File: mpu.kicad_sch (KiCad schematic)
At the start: 172 parts, among them J1 USB_OTG, J2 DIN41612_02x10_AB, J3 USB_OTG, J4 Conn_02x20_Counter_Clockwise, J5 Conn_01x15_Socket, U3 ECMF02-2AMX6, U4 ECMF02-2AMX6, U5 STM32MP157FADx, X1 ASE-24MHz

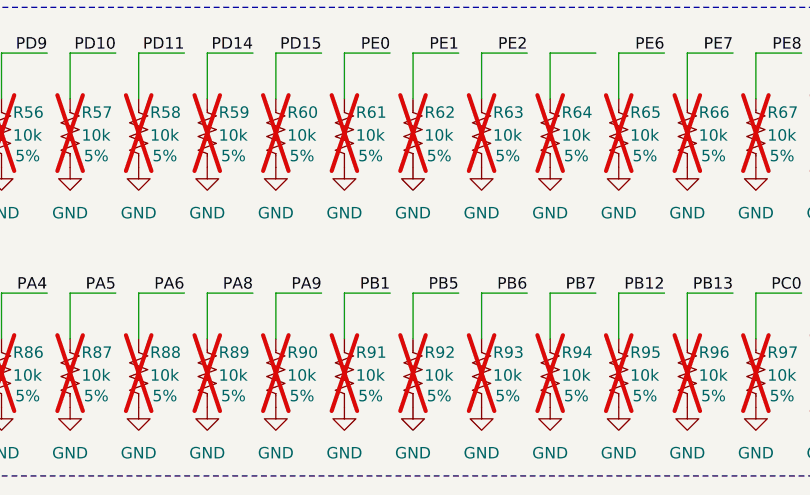
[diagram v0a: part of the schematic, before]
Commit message: Routing GPIOs
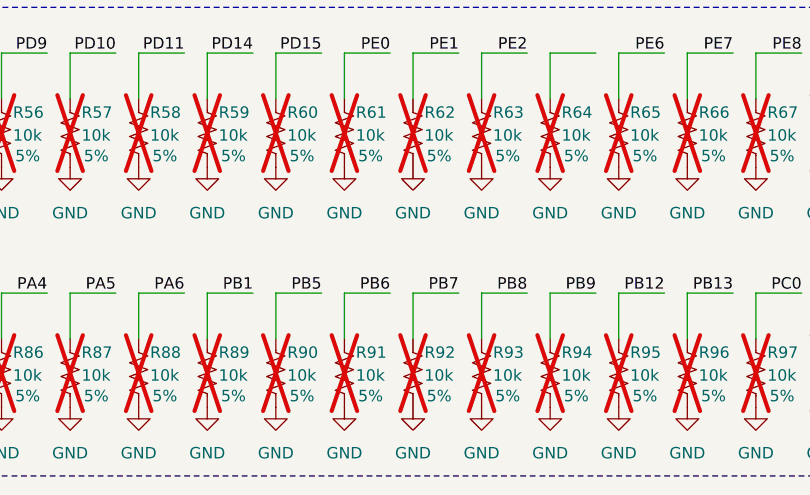
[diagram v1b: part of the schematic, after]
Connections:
- net PA9 is gone; now on net PB5: R90.1
- net PA8: no longer R89.1
- net PB1: now also R89.1; no longer R91.1
- net PB5: no longer R92.1
- net PB6: now also R91.1; no longer R93.1
- net PB7: now also R92.1; no longer R94.1
- net PB8: now also R93.1
- net PB9: now also R94.1
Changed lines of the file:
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@@
 		)
 	)
-	(label "PB7"
-		(at 95.25 397.51 180)
-		(fields_autoplaced yes)
-		(effects
-			(font
-				(size 1.27 1.27)
-			)
-			(justify right bottom)
-		)
-	)
 	(label "UART4_TX"
 		(at 326.39 229.87 0)
@@
 		)
 	)
-	(label "PB6"
-		(at 87.63 397.51 180)
-		(fields_autoplaced yes)
-		(effects
-			(font
-				(size 1.27 1.27)
-			)
-			(justify right bottom)
-		)
-	)
 	(label "PA5"
 		(at 326.39 227.33 0)
@@
 		)
 	)
-	(label "PB1"
-		(at 72.39 397.51 180)
-		(fields_autoplaced yes)
-		(effects
-			(font
-				(size 1.27 1.27)
-			)
-			(justify right bottom)
-		)
-	)
 	(label "PF10"
 		(at 209.55 370.84 180)
@@
 		)
 	)
+	(label "PB1"
+		(at 57.15 397.51 180)
+		(fields_autoplaced yes)
+		(effects
+			(font
+				(size 1.27 1.27)
+			)
+			(justify right bottom)
+		)
+	)
 	(label "nRST"
 		(at 496.57 105.41 0)
@@
 		)
 	)
+	(label "PB8"
+		(at 87.63 397.51 180)
+		(fields_autoplaced yes)
+		(effects
+			(font
+				(size 1.27 1.27)
+			)
+			(justify right bottom)
+		)
+	)
 	(label "A14"
 		(at 196.85 232.41 0)
@@
 		)
 	)
+	(label "PB5"
+		(at 64.77 397.51 180)
+		(fields_autoplaced yes)
+		(effects
+			(font
+				(size 1.27 1.27)
+			)
+			(justify right bottom)
+		)
+	)
 	(label "PC10"
 		(at 171.45 397.51 180)
@@
 		)
 	)
+	(label "PB9"
+		(at 95.25 397.51 180)
+		(fields_autoplaced yes)
+		(effects
+			(font
+				(size 1.27 1.27)
+			)
+			(justify right bottom)
+		)
+	)
 	(label "VDD_DDR"
 		(at 105.41 325.12 90)
@@
 		)
 	)
-	(label "PA8"
-		(at 57.15 397.51 180)
-		(fields_autoplaced yes)
-		(effects
-			(font
-				(size 1.27 1.27)
-			)
-			(justify right bottom)
-		)
-	)
 	(label "VDD_CORE"
 		(at 115.57 325.12 90)
@@
 		)
 	)
-	(label "PA9"
-		(at 64.77 397.51 180)
+	(label "PB7"
+		(at 80.01 397.51 180)
 		(fields_autoplaced yes)
 		(effects
@@
 		)
 	)
-	(label "PB5"
-		(at 80.01 397.51 180)
-		(fields_autoplaced yes)
-		(effects
-			(font
-				(size 1.27 1.27)
-			)
-			(justify right bottom)
-		)
-	)
 	(label "VDD1V1_REG"
 		(at 502.92 337.82 180)
@@
 		)
 	)
+	(label "PB6"
+		(at 72.39 397.51 180)
+		(fields_autoplaced yes)
+		(effects
+			(font
+				(size 1.27 1.27)
+			)
+			(justify right bottom)
+		)
+	)

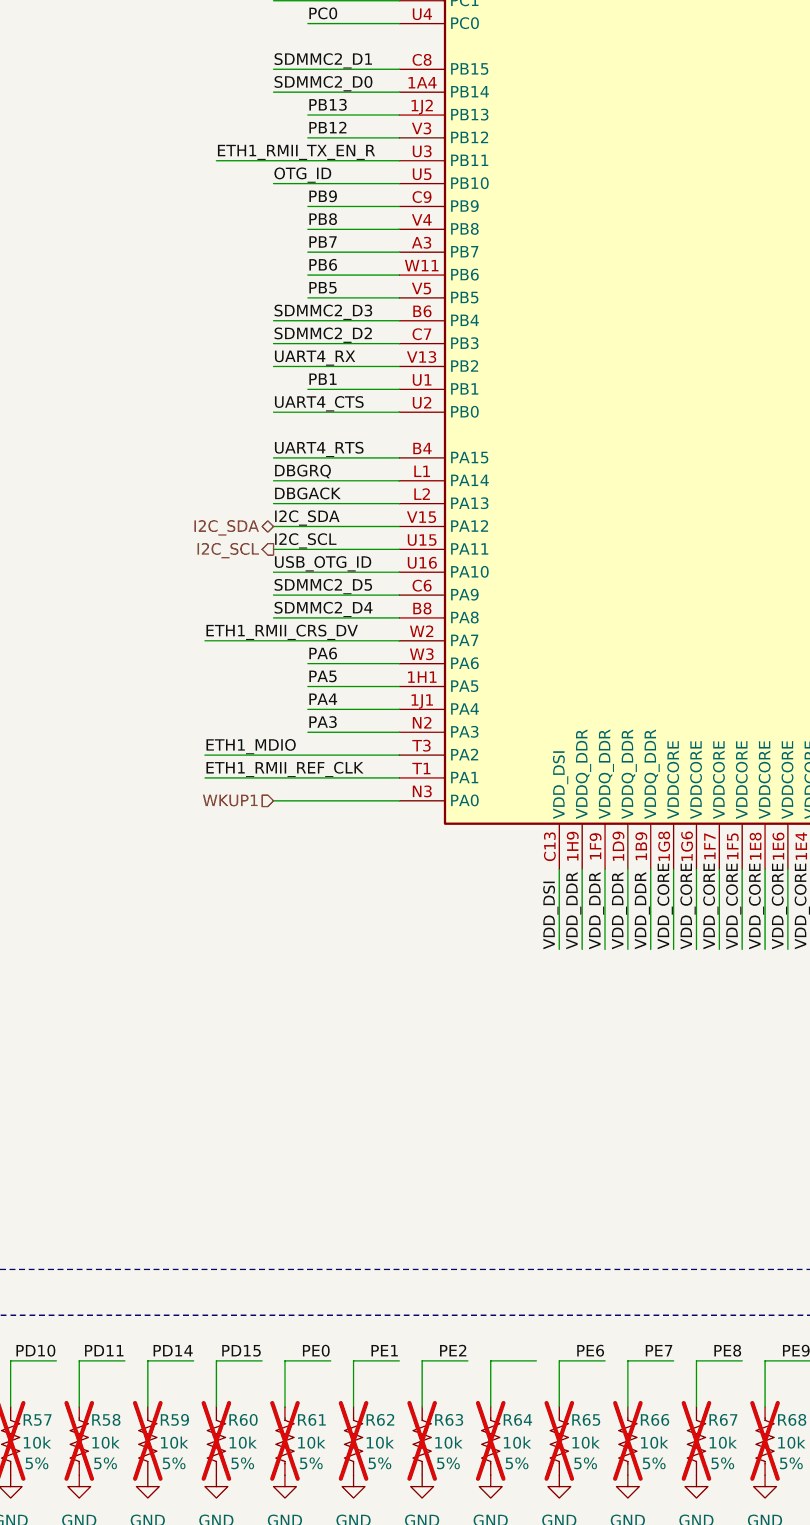
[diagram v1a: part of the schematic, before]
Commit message: Routed GPIOs
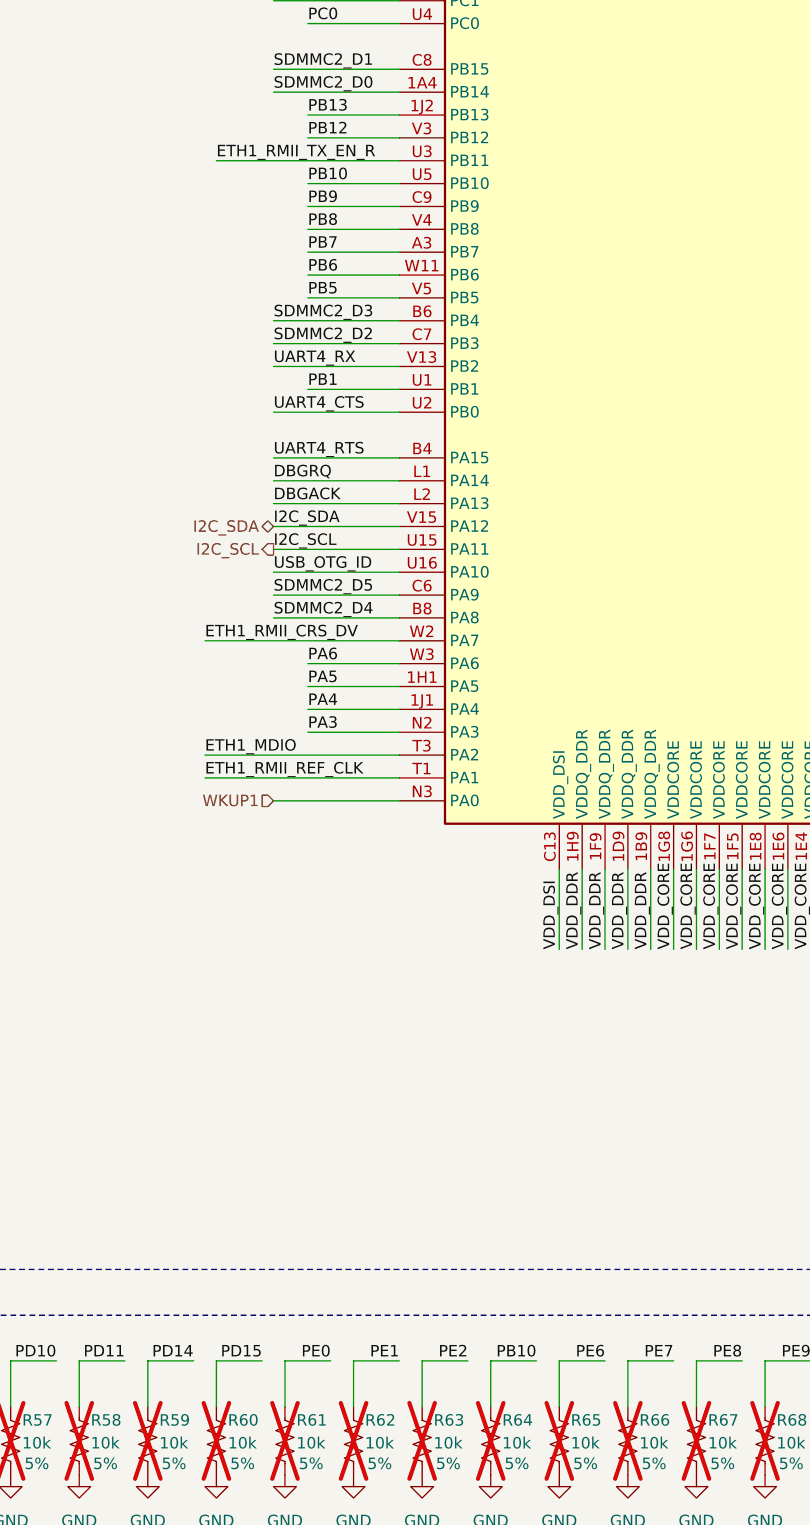
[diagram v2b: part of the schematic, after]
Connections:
- net OTG_ID is gone; now on net PB10: U5.U5 (PB10)
- net PB10: now reaches R64.1
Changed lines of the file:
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@@
 	(wire
 		(pts
-			(xy 66.04 240.03) (xy 80.01 240.03)
+			(xy 69.85 240.03) (xy 80.01 240.03)
 		)
 		(stroke
@@
 		)
 	)
+	(label "PB10"
+		(at 95.25 370.84 180)
+		(fields_autoplaced yes)
+		(effects
+			(font
+				(size 1.27 1.27)
+			)
+			(justify right bottom)
+		)
+	)
 	(label "DBGRQ"
 		(at 496.57 107.95 0)
@@
 		)
 	)
+	(label "PB10"
+		(at 69.85 240.03 0)
+		(fields_autoplaced yes)
+		(effects
+			(font
+				(size 1.27 1.27)
+			)
+			(justify left bottom)
+		)
+	)
 	(label "UART4_RX"
 		(at 384.81 389.89 0)
@@
 		(fields_autoplaced yes)
 		(effects
-			(font
-				(size 1.27 1.27)
-			)
-			(justify left bottom)
-		)
-	)
-	(label "OTG_ID"
-		(at 66.04 240.03 0)
-		(fields_autoplaced yes)
-		(effects

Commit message: Added decoupling back in and changed to 0201
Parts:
- C14, C15, C16, C17, C18, C19, C20, C21, C22, C23, C24, C25, C26, C27, C28, C29, C38, C39, C40, C41: footprint Capacitor_SMD:C_0402_1005Metric -> Capacitor_SMD:C_0201_0603Metric
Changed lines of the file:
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@@
 			)
 		)
-		(property "Footprint" "Capacitor_SMD:C_0402_1005Metric"
+		(property "Footprint" "Capacitor_SMD:C_0201_0603Metric"
 			(at 423.8752 302.26 0)
 			(effects
@@
 			)
 		)
-		(property "Footprint" "Capacitor_SMD:C_0402_1005Metric"
+		(property "Footprint" "Capacitor_SMD:C_0201_0603Metric"
 			(at 449.2752 251.46 0)
 			(effects
@@
 			)
 		)
-		(property "Footprint" "Capacitor_SMD:C_0402_1005Metric"
+		(property "Footprint" "Capacitor_SMD:C_0201_0603Metric"
 			(at 398.4752 302.26 0)
 			(effects
@@
 			)
 		)
-		(property "Footprint" "Capacitor_SMD:C_0402_1005Metric"
+		(property "Footprint" "Capacitor_SMD:C_0201_0603Metric"
 			(at 436.5752 251.46 0)
 			(effects
@@
 			)
 		)
-		(property "Footprint" "Capacitor_SMD:C_0402_1005Metric"
+		(property "Footprint" "Capacitor_SMD:C_0201_0603Metric"
 			(at 398.4752 251.46 0)
 			(effects
@@
 			)
 		)
-		(property "Footprint" "Capacitor_SMD:C_0402_1005Metric"
+		(property "Footprint" "Capacitor_SMD:C_0201_0603Metric"
 			(at 385.7752 226.06 0)
 			(effects
@@
 			)
 		)
-		(property "Footprint" "Capacitor_SMD:C_0402_1005Metric"
+		(property "Footprint" "Capacitor_SMD:C_0201_0603Metric"
 			(at 398.4752 226.06 0)
 			(effects
@@
 			)
 		)
-		(property "Footprint" "Capacitor_SMD:C_0402_1005Metric"
+		(property "Footprint" "Capacitor_SMD:C_0201_0603Metric"
 			(at 436.5752 226.06 0)
 			(effects
@@
 			)
 		)
-		(property "Footprint" "Capacitor_SMD:C_0402_1005Metric"
+		(property "Footprint" "Capacitor_SMD:C_0201_0603Metric"
 			(at 473.4052 251.46 0)
 			(effects
@@
 			)
 		)
-		(property "Footprint" "Capacitor_SMD:C_0402_1005Metric"
+		(property "Footprint" "Capacitor_SMD:C_0201_0603Metric"
 			(at 411.1752 251.46 0)
 			(effects
@@
 			)
 		)
-		(property "Footprint" "Capacitor_SMD:C_0402_1005Metric"
+		(property "Footprint" "Capacitor_SMD:C_0201_0603Metric"
 			(at 385.7752 302.26 0)
 			(effects
@@
 			)
 		)
-		(property "Footprint" "Capacitor_SMD:C_0402_1005Metric"
+		(property "Footprint" "Capacitor_SMD:C_0201_0603Metric"
 			(at 411.1752 302.26 0)
 			(effects
@@
 			)
 		)
-		(property "Footprint" "Capacitor_SMD:C_0402_1005Metric"
+		(property "Footprint" "Capacitor_SMD:C_0201_0603Metric"
 			(at 423.8752 251.46 0)
 			(effects
@@
 			)
 		)
-		(property "Footprint" "Capacitor_SMD:C_0402_1005Metric"
+		(property "Footprint" "Capacitor_SMD:C_0201_0603Metric"
 			(at 461.9752 251.46 0)
 			(effects
@@
 			)
 		)
-		(property "Footprint" "Capacitor_SMD:C_0402_1005Metric"
+		(property "Footprint" "Capacitor_SMD:C_0201_0603Metric"
 			(at 423.8752 226.06 0)
 			(effects
@@
 			)
 		)
-		(property "Footprint" "Capacitor_SMD:C_0402_1005Metric"
+		(property "Footprint" "Capacitor_SMD:C_0201_0603Metric"
 			(at 449.2752 226.06 0)
 			(effects
@@
 			)
 		)
-		(property "Footprint" "Capacitor_SMD:C_0402_1005Metric"
+		(property "Footprint" "Capacitor_SMD:C_0201_0603Metric"
 			(at 486.1052 251.46 0)
 			(effects
@@
 			)
 		)
-		(property "Footprint" "Capacitor_SMD:C_0402_1005Metric"
+		(property "Footprint" "Capacitor_SMD:C_0201_0603Metric"
 			(at 473.4052 226.06 0)
 			(effects
@@
 			)
 		)
-		(property "Footprint" "Capacitor_SMD:C_0402_1005Metric"
+		(property "Footprint" "Capacitor_SMD:C_0201_0603Metric"
 			(at 460.7052 226.06 0)
 			(effects
@@
 			)
 		)
-		(property "Footprint" "Capacitor_SMD:C_0402_1005Metric"
+		(property "Footprint" "Capacitor_SMD:C_0201_0603Metric"
 			(at 411.1752 226.06 0)
 			(effects

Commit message: Fixing some stuff
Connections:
- net VIN is gone; now on net VDD: J4.1 (Pin_1), J4.40 (Pin_40)
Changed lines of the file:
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@@
 		)
 	)
+	(label "VDD"
+		(at 367.03 218.44 0)
+		(fields_autoplaced yes)
+		(effects
+			(font
+				(size 1.27 1.27)
+			)
+			(justify left bottom)
+		)
+	)
 	(label "ETH1_RMII_TX_EN_R"
 		(at 312.42 102.87 0)
@@
 		)
 	)
+	(label "VDD"
+		(at 326.39 218.44 0)
+		(fields_autoplaced yes)
+		(effects
+			(font
+				(size 1.27 1.27)
+			)
+			(justify left bottom)
+		)
+	)
 	(label "PF9"
 		(at 69.85 85.09 0)
@@
 	)
 	(symbol
-		(lib_id "SparkFun-PowerSymbol:VIN")
-		(at 367.03 218.44 0)
-		(unit 1)
-		(exclude_from_sim no)
-		(in_bom yes)
-		(on_board yes)
-		(dnp no)
-		(fields_autoplaced yes)
-		(property "Reference" "#PWR093"
-			(at 367.03 222.25 0)
-			(effects
-				(font
-					(size 1.27 1.27)
-				)
-				(hide yes)
-			)
-		)
-		(property "Value" "VIN"
-			(at 367.03 214.63 0)
-			(do_not_autoplace yes)
-			(effects
-				(font
-					(size 1.27 1.27)
-				)
-			)
-		)
-		(property "Footprint" ""
-			(at 367.03 218.44 0)
-			(effects
-				(font
-					(size 1.27 1.27)
-				)
-				(hide yes)
-			)
-		)
-		(property "Datasheet" ""
-			(at 367.03 218.44 0)
-			(effects
-				(font
-					(size 1.27 1.27)
-				)
-				(hide yes)
-			)
-		)
-		(property "Description" "Power symbol creates a global label with name \"VIN\""
-			(at 367.03 218.44 0)
-			(effects
-				(font
-					(size 1.27 1.27)
-				)
-				(hide yes)
-			)
-		)
-		(pin "1"
-		)
-		(instances
-			(project "SBC"
-				(path "/21bb932a-ec67-4661-9215-0551f718d1c0/3336208b-c91e-4833-a187-5ed2272e0a27"
-					(reference "#PWR093")
-					(unit 1)
-				)
-			)
-		)
-	)
-	(symbol
 		(lib_id "SparkFun-Resistor:R")
 		(at 219.71 406.4 90)
@@
 					(unit 1)
 				)
-			)
-		)
-	)
-	(symbol
-		(lib_id "SparkFun-PowerSymbol:VIN")
-		(at 326.39 218.44 0)
-		(unit 1)
-		(exclude_from_sim no)
-		(in_bom yes)
-		(on_board yes)
-		(dnp no)
-		(fields_autoplaced yes)
-		(property "Reference" "#PWR092"
-			(at 326.39 222.25 0)
-			(effects
-				(font
-					(size 1.27 1.27)
-				)
-				(hide yes)
-			)
-		)
-		(property "Value" "VIN"
-			(at 326.39 214.63 0)
-			(do_not_autoplace yes)
-			(effects
-				(font
-					(size 1.27 1.27)
-				)
-			)
-		)
-		(property "Footprint" ""
-			(at 326.39 218.44 0)
-			(effects
-				(font
-					(size 1.27 1.27)
-				)
-				(hide yes)
-			)
-		)
-		(property "Datasheet" ""
-			(at 326.39 218.44 0)
-			(effects
-				(font
-					(size 1.27 1.27)
-				)
-				(hide yes)
-			)
-		)
-		(property "Description" "Power symbol creates a global label with name \"VIN\""
-			(at 326.39 218.44 0)
-			(effects
-				(font
-					(size 1.27 1.27)
-				)
-				(hide yes)
-			)
-		)
-		(pin "1"
-		)
-		(instances
-			(project "SBC"
-				(path "/21bb932a-ec67-4661-9215-0551f718d1c0/3336208b-c91e-4833-a187-5ed2272e0a27"
-					(reference "#PWR092")
-					(unit 1)
-				)

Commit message: Incremental changes
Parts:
- removed NT4, NT5: NetTie_2, NetTie:NetTie-2_SMD_Pad0.5mm, symbol Device:NetTie_2
- C50, C51, C52: footprint Capacitor_SMD:C_0402_1005Metric -> Capacitor_SMD:C_0201_0603Metric
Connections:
- net VDD_USB is gone; now on net VDD3V3_USB: U5.1H7 (VDD3V3_USB)
- net VREF+ is gone; now on net VDDA: C55.1, C56.1, U5.M3 (VREF+)
- net VSSA is gone; now on net GND: C53.2, C54.2, C55.2, C56.2, U5.1G1 (VSSA)
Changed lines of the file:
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@@
 	(generator_version "8.0")
 	(paper "C")
+	(bus_alias "GND"
+		(members "VSSA")
+	)
+	(bus_alias "VREF+"
+		(members "VDDA")
+	)
 	(junction
 		(at 435.61 210.82)
@@
 	(wire
 		(pts
-			(xy 476.25 363.22) (xy 480.06 363.22)
+			(xy 476.25 363.22) (xy 488.95 363.22)
 		)
 		(stroke
@@
 	(wire
 		(pts
-			(xy 485.14 363.22) (xy 488.95 363.22)
-		)
-		(stroke
-			(width 0)
-			(type default)
-		)
-	)
-	(wire
-		(pts
 			(xy 212.09 370.84) (xy 217.17 370.84)
 		)
@@
 	(wire
 		(pts
-			(xy 158.75 316.23) (xy 158.75 325.12)
+			(xy 158.75 316.23) (xy 158.75 328.93)
 		)
 		(stroke
@@
 	(wire
 		(pts
-			(xy 435.61 363.22) (xy 448.31 363.22)
+			(xy 435.61 363.22) (xy 461.01 363.22)
 		)
 		(stroke
@@
 	(wire
 		(pts
-			(xy 453.39 363.22) (xy 461.01 363.22)
-		)
-		(stroke
-			(width 0)
-			(type default)
-		)
-	)
-	(wire
-		(pts
 			(xy 196.85 148.59) (xy 209.55 148.59)
 		)
@@
 		)
 	)
+	(label "VDD3V3_USB"
+		(at 158.75 328.93 90)
+		(fields_autoplaced yes)
+		(effects
+			(font
+				(size 1.27 1.27)
+			)
+			(justify left bottom)
+		)
+	)
 	(label "PA3"
 		(at 69.85 300.99 0)
@@
 		)
 	)
-	(label "VDD_USB"
-		(at 158.75 325.12 90)
-		(fields_autoplaced yes)
-		(effects
-			(font
-				(size 1.27 1.27)
-			)
-			(justify left bottom)
-		)
-	)
 	(label "PG10"
 		(at 240.03 370.84 180)
@@
 	)
 	(symbol
-		(lib_id "Device:NetTie_2")
-		(at 450.85 363.22 180)
-		(unit 1)
-		(exclude_from_sim no)
-		(in_bom no)
-		(on_board yes)
-		(dnp no)
-		(fields_autoplaced yes)
-		(property "Reference" "NT4"
-			(at 449.5799 361.95 90)
-			(effects
-				(font
-					(size 1.27 1.27)
-				)
-				(justify right)
-			)
-		)
-		(property "Value" "NetTie_2"
-			(at 452.1199 361.95 90)
-			(effects
-				(font
-					(size 1.27 1.27)
-				)
-				(justify right)
-			)
-		)
-		(property "Footprint" "NetTie:NetTie-2_SMD_Pad0.5mm"
-			(at 450.85 363.22 0)
-			(effects
-				(font
-					(size 1.27 1.27)
-				)
-				(hide yes)
-			)
-		)
-		(property "Datasheet" "~"
-			(at 450.85 363.22 0)
-			(effects
-				(font
-					(size 1.27 1.27)
-				)
-				(hide yes)
-			)
-		)
-		(property "Description" "Net tie, 2 pins"
-			(at 450.85 363.22 0)
-			(effects
-				(font
-					(size 1.27 1.27)
-				)
-				(hide yes)
-			)
-		)
-		(pin "2"
-		)
-		(pin "1"
-		)
-		(instances
-			(project "SBC"
-				(path "/21bb932a-ec67-4661-9215-0551f718d1c0/3336208b-c91e-4833-a187-5ed2272e0a27"
-					(reference "NT4")
-					(unit 1)
-				)
-			)
-		)
-	)
-	(symbol
 		(lib_id "SparkFun-Resistor:R")
 		(at 105.41 379.73 90)
@@
 	)
 	(symbol
-		(lib_id "Device:NetTie_2")
-		(at 482.6 363.22 180)
-		(unit 1)
-		(exclude_from_sim no)
-		(in_bom no)
-		(on_board yes)
-		(dnp no)
-		(fields_autoplaced yes)
-		(property "Reference" "NT5"
-			(at 481.3299 361.95 90)
-			(effects
-				(font
-					(size 1.27 1.27)
-				)
-				(justify right)
-			)
-		)
-		(property "Value" "NetTie_2"
-			(at 483.8699 361.95 90)
-			(effects
-				(font
-					(size 1.27 1.27)
-				)
-				(justify right)
-			)
-		)
-		(property "Footprint" "NetTie:NetTie-2_SMD_Pad0.5mm"
-			(at 482.6 363.22 0)
-			(effects
-				(font
-					(size 1.27 1.27)
-				)
-				(hide yes)
-			)
-		)
-		(property "Datasheet" "~"
-			(at 482.6 363.22 0)
-			(effects
-				(font
-					(size 1.27 1.27)
-				)
-				(hide yes)
-			)
-		)
-		(property "Description" "Net tie, 2 pins"
-			(at 482.6 363.22 0)
-			(effects
-				(font
-					(size 1.27 1.27)
-				)
-				(hide yes)
-			)
-		)
-		(pin "2"
-		)
-		(pin "1"
-		)
-		(instances
-			(project "SBC"
-				(path "/21bb932a-ec67-4661-9215-0551f718d1c0/3336208b-c91e-4833-a187-5ed2272e0a27"
-					(reference "NT5")
-					(unit 1)
-				)
-			)
-		)
-	)
-	(symbol
 		(lib_id "power:GND")
 		(at 384.81 320.04 0)
@@
 			)
 		)
-		(property "Footprint" "Capacitor_SMD:C_0402_1005Metric"
+		(property "Footprint" "Capacitor_SMD:C_0201_0603Metric"
 			(at 460.7052 353.06 0)
 			(effects
@@
 			)
 		)
-		(property "Footprint" "Capacitor_SMD:C_0402_1005Metric"
+		(property "Footprint" "Capacitor_SMD:C_0201_0603Metric"
 			(at 486.1052 353.06 0)
 			(effects
@@
 			)
 		)
-		(property "Footprint" "Capacitor_SMD:C_0402_1005Metric"
+		(property "Footprint" "Capacitor_SMD:C_0201_0603Metric"
 			(at 512.7752 353.06 0)
 			(effects

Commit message: Everything is placed
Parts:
- removed C54: 100nF, Capacitor_SMD:C_0402_1005Metric, symbol SparkFun-Capacitor:C
- removed TP17, TP18, TP19: TestPoint, SparkFun-Connector:TestPoint-0.5mm, symbol Connector:TestPoint
- C45, C56: footprint Capacitor_SMD:C_0402_1005Metric -> Capacitor_SMD:C_0201_0603Metric
- R41: footprint Resistor_SMD:R_0402_1005Metric -> Resistor_SMD:R_0201_0603Metric

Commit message: Initial routing complete
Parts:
- C30, C31: footprint Capacitor_SMD:C_0402_1005Metric -> Capacitor_SMD:C_0201_0603Metric
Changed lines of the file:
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@@
 			)
 		)
-		(property "Footprint" "Capacitor_SMD:C_0402_1005Metric"
+		(property "Footprint" "Capacitor_SMD:C_0201_0603Metric"
 			(at 398.4752 276.86 0)
 			(effects
@@
 			)
 		)
-		(property "Footprint" "Capacitor_SMD:C_0402_1005Metric"
+		(property "Footprint" "Capacitor_SMD:C_0201_0603Metric"
 			(at 385.7752 276.86 0)
 			(effects
